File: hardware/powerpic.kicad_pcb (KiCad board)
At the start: 2 copper layers, 25.6 x 27.6 mm, 17 parts, among them U1 PIC16LF1919x-I/MR

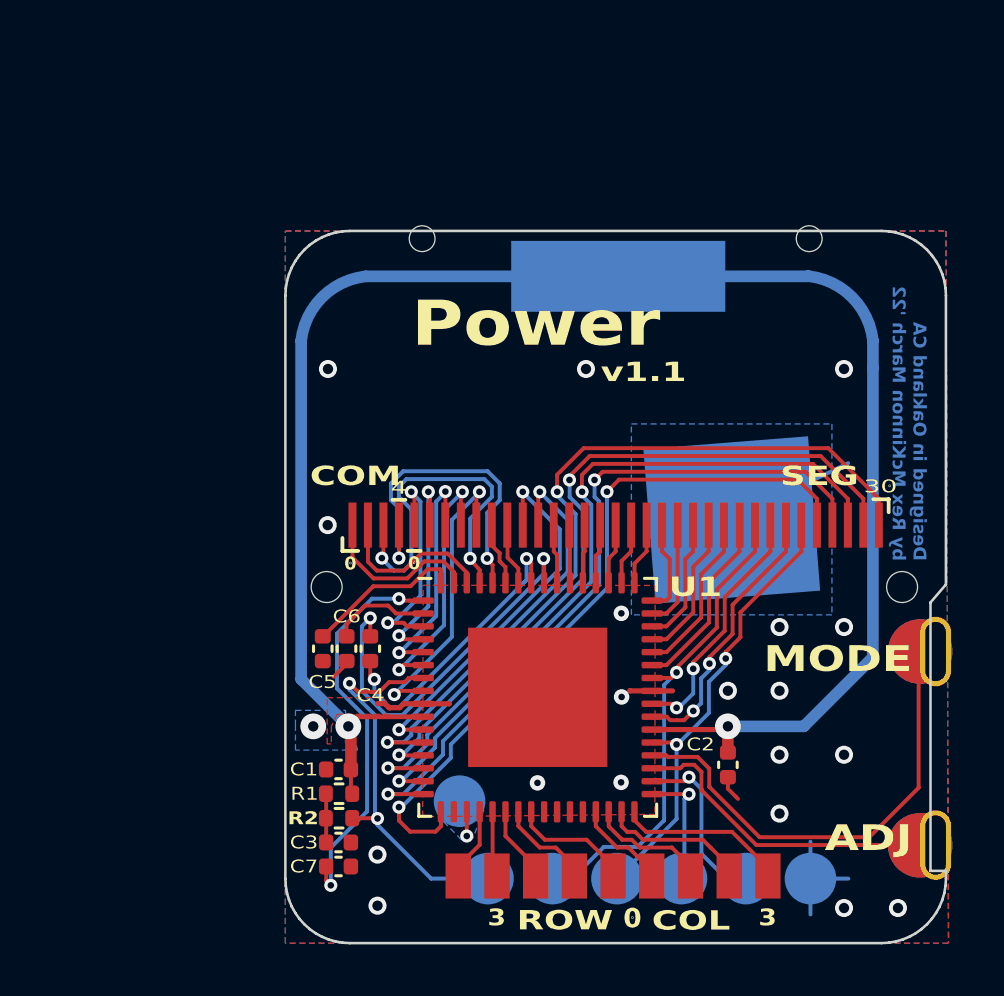
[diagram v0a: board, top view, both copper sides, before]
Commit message: Redesigned board with RTCXTAL and led backlight
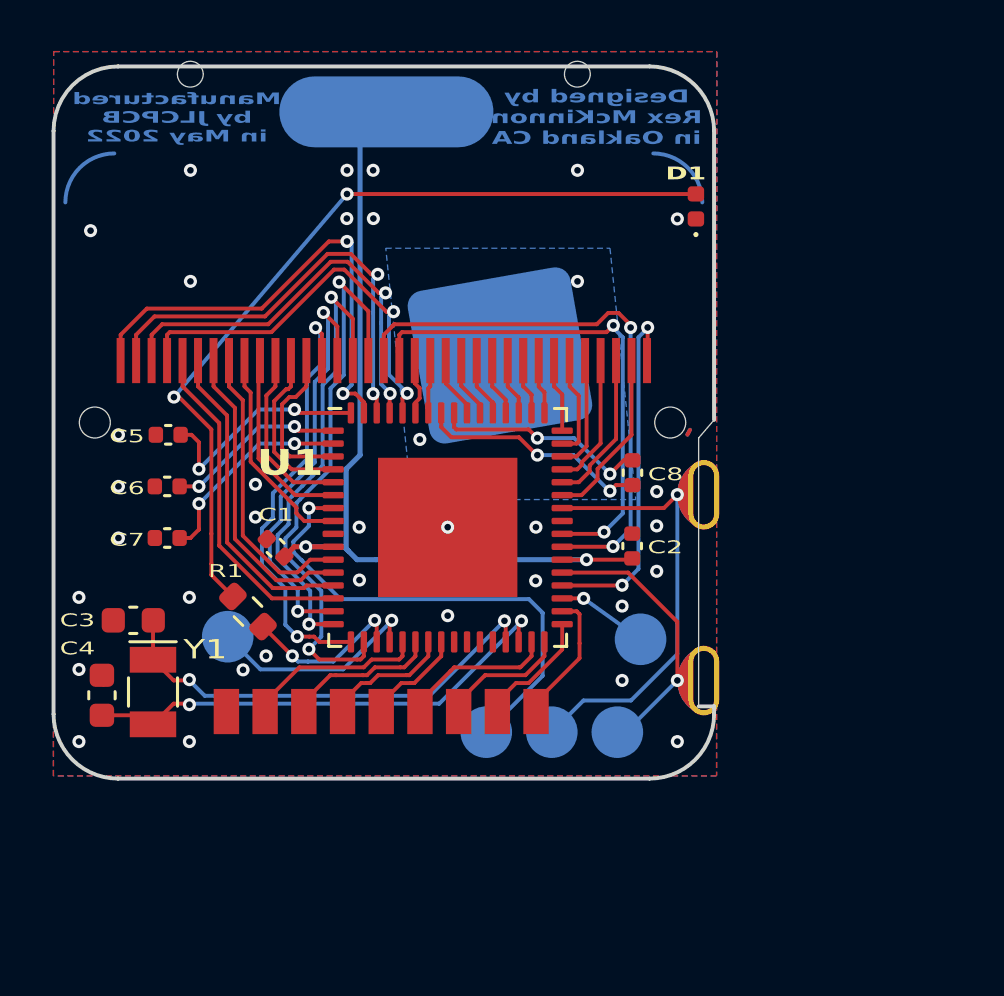
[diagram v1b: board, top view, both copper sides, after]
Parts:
- removed GND: Progo_Pad_D2.0mm, powerpic:Progo_Pad_D2.0mm
- removed R2: 100Ω, Resistor_SMD:R_0402_1005Metric
- removed TP5: UART_TX, powerpic:Progo_Pad_D2.0mm
- added C8: 1μF, Capacitor_SMD:C_0402_1005Metric, F.Cu at (140.4, 58.0)
- added D1: LCD_LED, LED_SMD:LED_0402_1005Metric, F.Cu at (142.9, 47.6)
- added Y1: 32.768kHz, Crystal:Crystal_SMD_MicroCrystal_CC7V-T1A-2Pin_3.2x1.5mm, F.Cu at (121.9, 66.5)
- C3: value 10nF -> TBD; footprint Capacitor_SMD:C_0402_1005Metric -> Capacitor_SMD:C_0603_1608Metric
- C4: value 1μF -> TBD; footprint Capacitor_SMD:C_0402_1005Metric -> Capacitor_SMD:C_0603_1608Metric
- C7: value NC -> 0.27μF
- R1: value 100Ω -> TBD; footprint Resistor_SMD:R_0402_1005Metric -> Resistor_SMD:R_0603_1608Metric
- TP2: value ICSP_CLK -> Mode
- TP3: value ICSP_DAT -> Adj
- TP4: value UART_RX -> Debug
- moved C7 14.4 mm to (122.4, 60.5), turned to 180 degrees
- moved C3 11.7 mm to (121.1, 63.7)
- moved PPC1 11.0 mm to (118.0, 69.8)
- moved C4 10.6 mm to (119.9, 66.6)
- moved C5 10.2 mm to (122.5, 56.5), turned to 180 degrees
- moved TP4 9.41 mm to (140.8, 64.4)
- moved C6 9.37 mm to (122.4, 58.5), turned to 180 degrees
- moved C2 9.26 mm to (140.4, 60.8), turned to -90 degrees
- moved C1 8.93 mm to (126.6, 60.9), turned to -45 degrees
- moved R1 7.89 mm to (125.5, 63.4), turned to -45 degrees
- moved U1 7.45 mm to (133.3, 60.1)
- moved TP1 5.68 mm to (134.8, 68.0)
- moved TP2 5.68 mm to (137.3, 68.0)
- moved TP3 5.68 mm to (139.9, 68.0)
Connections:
- C3 pad 1: GND -> /SOSCI
- C3 pad 2: Net-(C3-Pad2) -> GND
- C4 pad 1: /CFLY1 -> /SOSCO
- C4 pad 2: /CFLY2 -> GND
- C6 pad 1: /VLCD1 -> /VLCD2
- C7 pad 1: /VLCD2 -> /VLCD1
- PPC1 pad 6: /KTEST -> GND
- R1 pad 1: Net-(C3-Pad2) -> Net-(D1-A)
- R1 pad 2: VCC -> /LIGHT
- TP2 pad 1: /SEG22 -> /MODE
- TP3 pad 1: /SEG25 -> /ADJ
- TP4 pad 1: /UART_RX -> /DEBUG
- U1 pad 11: /SEG7 -> /SEG3
- U1 pad 12: /SEG8 -> /SEG2
- U1 pad 13: /SEG30 -> /SEG1
- U1 pad 14: /SEG29 -> /SEG0
- U1 pad 15: /SEG28 -> /SEG10
- U1 pad 16: /SEG27 -> /SEG11
- U1 pad 17: /SEG26 -> /SEG9
- U1 pad 18: unconnected-(U1-SEG41/RF0) -> /SEG12
- U1 pad 19: /BUZZ -> /LIGHT
- U1 pad 20: /KTEST -> /BUZZ
- U1 pad 29: /COL0 -> /SOSCI
- U1 pad 3: /SEG0 -> /SEG8
- U1 pad 30: /COL1 -> /SOSCO
- U1 pad 31: /COL2 -> /COL0
- U1 pad 32: /COL3 -> /COL1
- U1 pad 33: /UART_RX -> /COL2
- U1 pad 34: /UART_TX -> /COL3
- U1 pad 35: /ADJ -> /DEBUG
- U1 pad 36: /MODE -> /SEG30
- U1 pad 37: /SEG25 -> /ADJ
- U1 pad 39: /SEG24 -> /SEG13
- U1 pad 4: /SEG1 -> /SEG7
- U1 pad 40: /SEG23 -> /SEG14
- U1 pad 42: /SEG22 -> /MODE
- U1 pad 43: /SEG21 -> /SEG29
- U1 pad 44: /SEG20 -> /SEG28
- U1 pad 45: /SEG19 -> /SEG27
- U1 pad 46: /SEG18 -> /SEG26
- U1 pad 47: /SEG17 -> /SEG25
- U1 pad 48: /SEG16 -> /SEG24
- U1 pad 49: /SEG15 -> /SEG23
- U1 pad 5: /SEG2 -> /SEG6
- U1 pad 50: /SEG14 -> /SEG22
- U1 pad 51: /SEG13 -> /SEG21
- U1 pad 52: /SEG12 -> /SEG20
- U1 pad 53: /SEG11 -> /SEG19
- U1 pad 54: /SEG10 -> /SEG18
- U1 pad 55: /SEG9 -> /SEG17
- U1 pad 58: /SEG6 -> /SEG16
- U1 pad 59: /SEG5 -> /SEG15
- U1 pad 6: /SEG3 -> /SEG5
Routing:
- net VCC: track 69.4 -> 35.0 mm
- net Net-(D1-A): track 0.00 -> 32.7 mm, vias 0 -> 2
- net /SEG26: track 28.3 -> 4.45 mm, vias 2 -> 0
- net /SEG29: track 29.8 -> 6.77 mm, vias 2 -> 0
- net /SEG27: track 28.2 -> 5.17 mm, vias 2 -> 0
- net /SEG28: track 28.2 -> 5.96 mm, vias 2 -> 0
- net /SEG12: track 2.31 -> 22.4 mm, vias 0 -> 2
- net /SEG13: track 2.35 -> 22.0 mm, vias 0 -> 2
- net /SOSCO: track 0.00 -> 18.9 mm, vias 0 -> 2
- net /SOSCI: track 0.00 -> 17.8 mm, vias 0 -> 2
- net /SEG14: track 2.39 -> 19.6 mm, vias 0 -> 2
- net /SEG22: track 19.2 -> 2.16 mm, vias 1 -> 0
- net /SEG30: track 29.7 -> 14.0 mm
- net /SEG11: track 2.27 -> 18.0 mm, vias 0 -> 2
- net /SEG9: track 2.29 -> 17.1 mm, vias 0 -> 2
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- removed copper zone on B.Cu, net /BUZZ
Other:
- outline, holes or cut-outs redrawn
- board text added: "2.0"
- board text added: "C"
- board text added: "D"
- board text added: "DBG"
- board text added: "Designed by Rex McKinnon in Oakland CA"
- board text added: "ICSP"
- board text added: "Manufactured by JLCPCB in May 2022"
- board text added: "PowerPIC"
- board text added: "R"
- board text removed: "0"
- board text removed: "3"
- board text removed: "30"
- board text removed: "4"
- board text removed: "ADJ"
- board text removed: "CLK"
- board text removed: "COL"
- board text removed: "COM"
- board text removed: "DAT"
- board text removed: "Designed in Oakland CA by Rex McKinnon March '22"
- board text removed: "MCLR"
- board text removed: "MODE"
- board text removed: "PIC"
- board text removed: "Power"
- board text removed: "ROW"
- board text removed: "RX"
- board text removed: "SEG"
- board text removed: "TX"
- board text removed: "v1.1"

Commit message: release version 2.1
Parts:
- removed TP1: ~{MCLR}, powerpic:Progo_Pad_D2.0mm
- removed TP2: Mode, powerpic:Progo_Pad_D2.0mm
- removed TP3: Adj, powerpic:Progo_Pad_D2.0mm
- removed TP4: Debug, powerpic:Progo_Pad_D2.0mm
- added kibuzzard-6619F1C8: G***, kibuzzard-6619F1C8, B.Cu at (134.2, 67.7)
- added kibuzzard-6619F370: G***, kibuzzard-6619F370, B.Cu at (140.3, 61.6)
- added kibuzzard-6619F3FA: G***, kibuzzard-6619F3FA, B.Cu at (136.2, 64.0)
- added kibuzzard-6619F45C: G***, kibuzzard-6619F45C, B.Cu at (122.3, 62.6)
- added kibuzzard-6619F682: G***, kibuzzard-6619F682, B.Cu at (133.9, 49.7)
- added kibuzzard-6619F6E4: G***, kibuzzard-6619F6E4, B.Cu at (131.0, 46.7)
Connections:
- U1 pad 25: /RH1 -> unconnected-(U1-COM5/RH1-Pad25)
- U1 pad 26: /RH0 -> unconnected-(U1-COM4/RH0-Pad26)
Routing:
- net /BUZZ: track 8.55 -> 14.2 mm
- net /DEBUG: track 3.55 -> 2.90 mm
- net /~{MCLR}: track 19.1 -> 19.6 mm
- net GND: vias 35 -> 38
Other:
- outline, holes or cut-outs redrawn
- board text added: "2416"
- board text added: "REXCM"
- board text added: "v2.1"
- board text removed: "2.0"
- board text removed: "BUZ"
- board text removed: "DBG"
- board text removed: "Designed by Rex McKinnon in Oakland CA"
- board text removed: "GND"
- board text removed: "ICSP"
- board text removed: "Manufactured by JLCPCB in May 2022"
- board text removed: "VIN"
